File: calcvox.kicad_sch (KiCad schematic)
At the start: 146 parts, among them J1 AudioJack2_Ground_Switch, SW1 RotaryEncoder_Switch, SW10 SW_Push, SW11 SW_Push, SW12 SW_Push, SW13 SW_Push, SW14 SW_Push, SW15 SW_Push, SW16 SW_Push, SW17 SW_Push, SW18 SW_Push, SW19 SW_Push, SW2 SW_Push, SW20 SW_Push, SW21 SW_Push, SW22 SW_Push, SW23 SW_Push, SW24 SW_Push, SW25 SW_Push, SW26 SW_Push, SW27 SW_Push, SW28 SW_Push, SW29 SW_Push, SW3 SW_Push, SW30 SW_Push, SW31 SW_Push, SW32 SW_Push, SW33 SW_Push, SW34 SW_Push, SW35 SW_Push, SW36 SW_Push, SW37 SW_Push, SW38 SW_Push, SW39 SW_Push, SW4 SW_Push, SW40 SW_Push, SW41 SW_Push, SW42 SW_Push, SW43 SW_Push, SW44 SW_Push, SW45 SW_Push, SW46 SW_Push, SW47 SW_Push, SW48 SW_Push, SW49 SW_Push, SW5 SW_Push, SW50 SW_Push, SW51 SW_Push, SW52 SW_Push, SW53 SW_Push, SW54 SW_Push, SW55 SW_Push, SW56 SW_Push, SW57 SW_Push, SW58 SW_Push, SW59 SW_Push, SW6 SW_Push, SW60 SW_Push, SW61 SW_Push, SW62 SW_Push, SW63 SW_Push, SW64 SW_Push, SW65 SW_Push, SW66 SW_Push, SW67 SW_SPDT, SW7 SW_Push, SW8 SW_Push, SW9 SW_Push

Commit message: added new changes
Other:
- note added: "CalcVox"

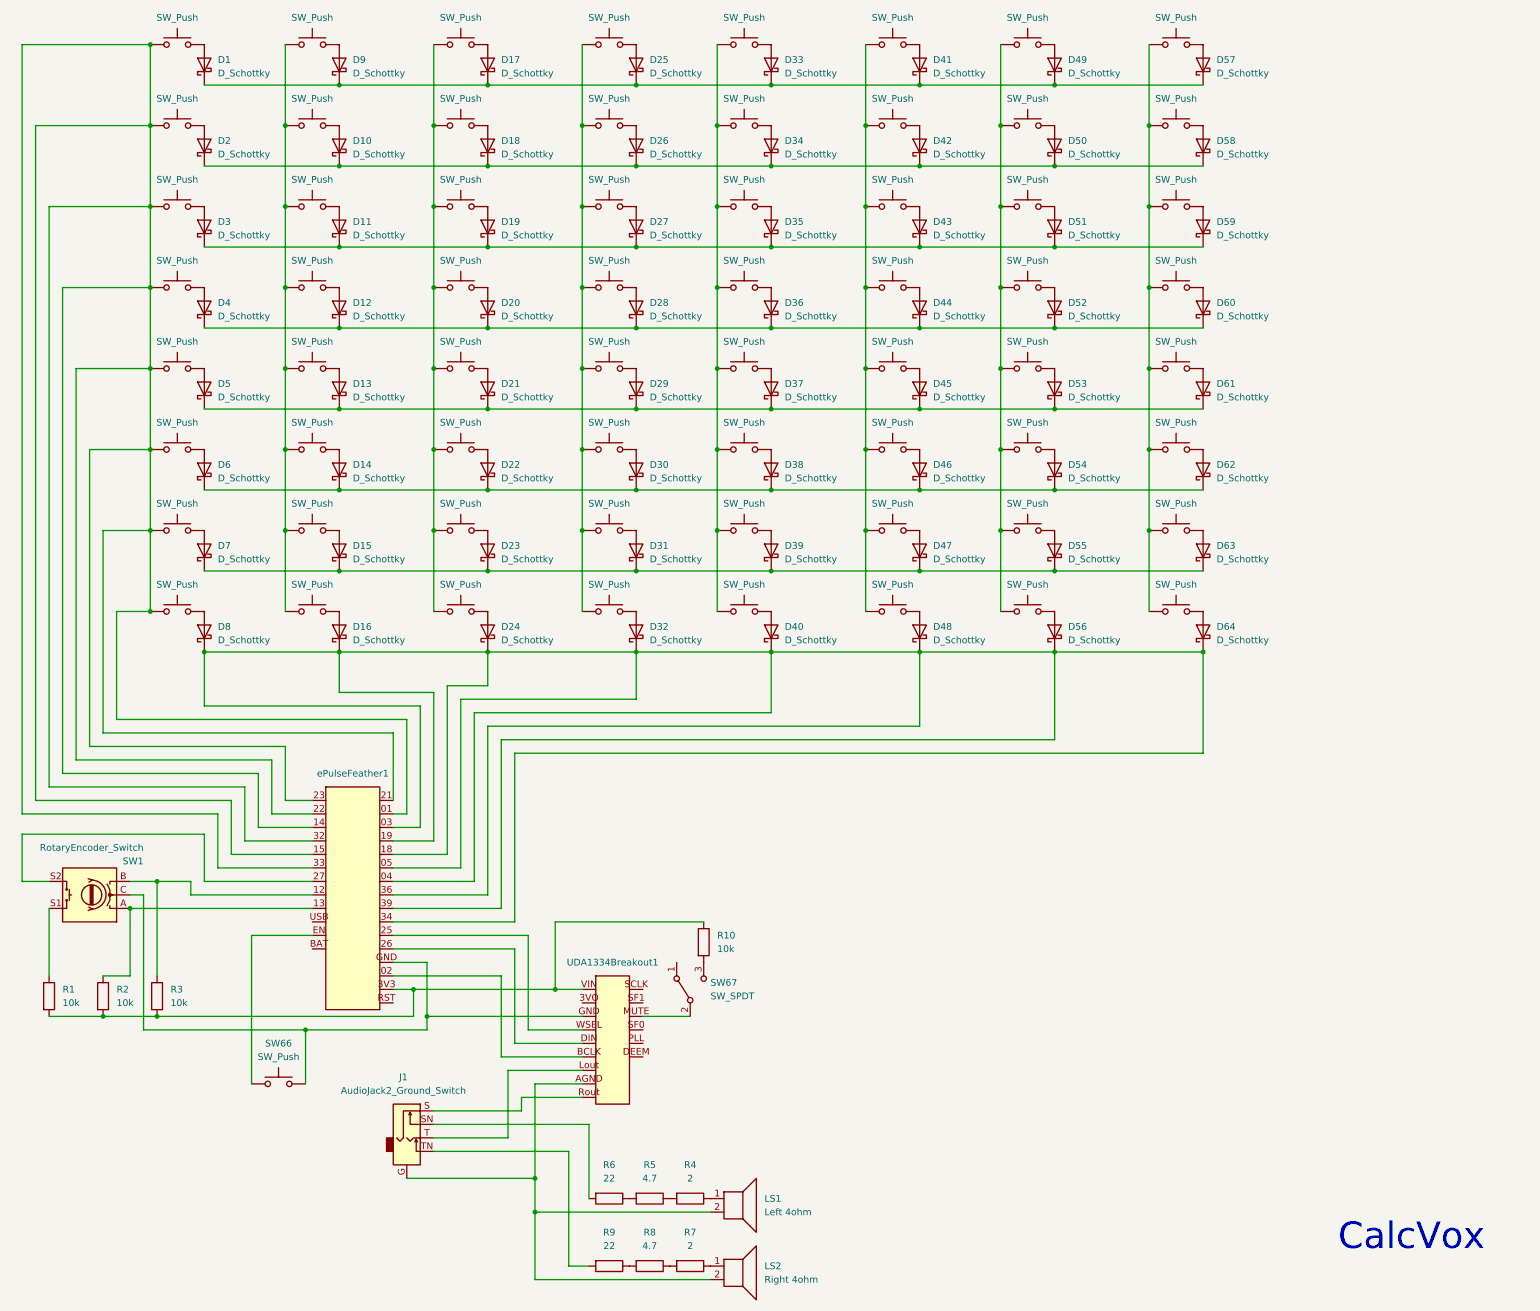
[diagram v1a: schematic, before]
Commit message: updated schematics
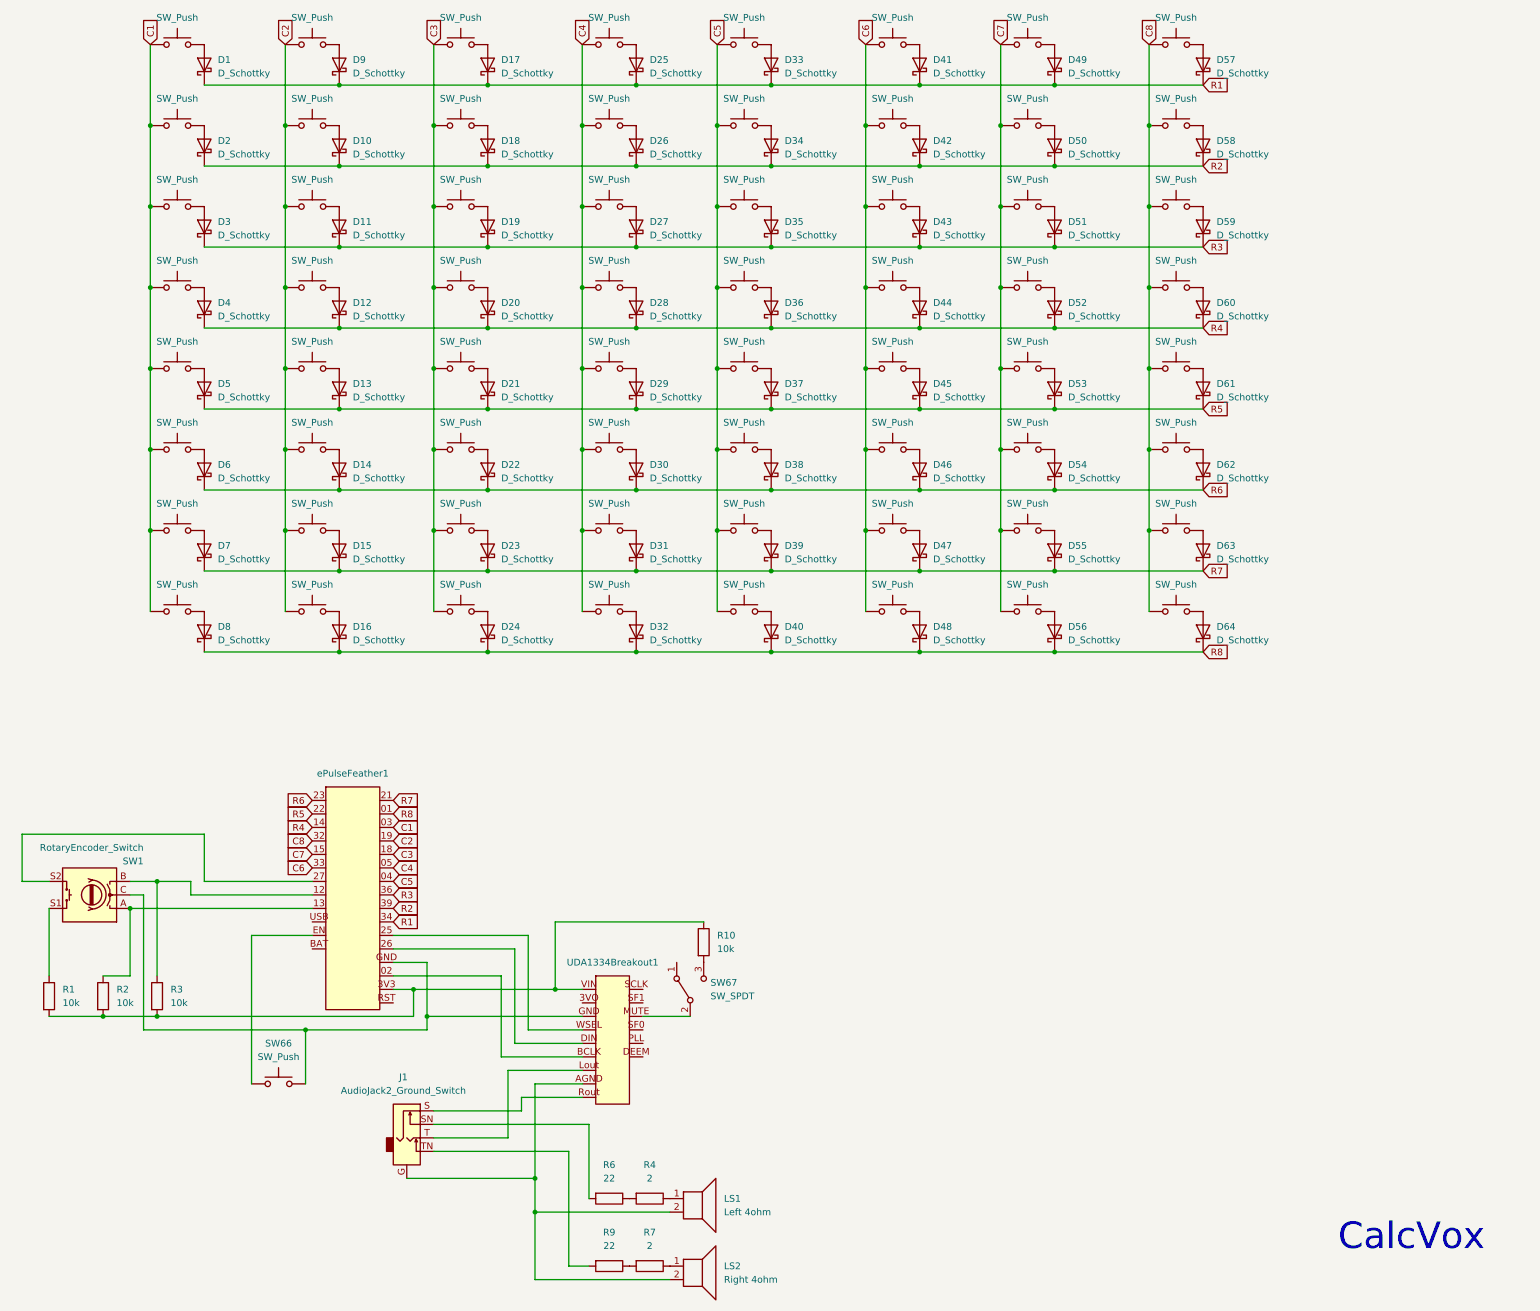
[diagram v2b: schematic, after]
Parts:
- removed R5, R8: 4.7, Resistor_THT:R_Axial_DIN0207_L6.3mm_D2.5mm_P7.62mm_Horizontal, symbol Device:R
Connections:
- net C4: now reaches SW26.1, SW27.1, SW28.1, SW29.1, SW30.1, SW31.1, SW32.1, SW33.1
- net C4: now also ePulseFeather1.05
- net R4: now reaches D12.1 (K), D20.1 (K), D28.1 (K), D36.1 (K), D4.1 (K), D44.1 (K), D52.1 (K), D60.1 (K)
- net R4: now also ePulseFeather1.14
- net R7: now reaches D15.1 (K), D23.1 (K), D31.1 (K), D39.1 (K), D47.1 (K), D55.1 (K), D63.1 (K), D7.1 (K)
- net R7: now also ePulseFeather1.21
- net R5: now reaches D13.1 (K), D21.1 (K), D29.1 (K), D37.1 (K), D45.1 (K), D5.1 (K), D53.1 (K), D61.1 (K)
- net R5: now also ePulseFeather1.22
- net R8: now reaches D16.1 (K), D24.1 (K), D32.1 (K), D40.1 (K), D48.1 (K), D56.1 (K), D64.1 (K), D8.1 (K)
- net R8: now also ePulseFeather1.01; no longer ePulseFeather1.03, ePulseFeather1.04, ePulseFeather1.05, ePulseFeather1.18, ePulseFeather1.19, ePulseFeather1.34, ePulseFeather1.36, ePulseFeather1.39
- net R2: now reaches D10.1 (K), D18.1 (K), D2.1 (K), D26.1 (K), D34.1 (K), D42.1 (K), D50.1 (K), D58.1 (K)
- net R2: now also ePulseFeather1.39
- net R1: now reaches D1.1 (K), D17.1 (K), D25.1 (K), D33.1 (K), D41.1 (K), D49.1 (K), D57.1 (K), D9.1 (K)
- net R1: now also ePulseFeather1.34
- net C1: now reaches SW2.1, SW3.1, SW4.1, SW5.1, SW6.1, SW7.1, SW8.1, SW9.1
- net C1: now also ePulseFeather1.03; no longer ePulseFeather1.01, ePulseFeather1.14, ePulseFeather1.15, ePulseFeather1.21, ePulseFeather1.22, ePulseFeather1.23, ePulseFeather1.32, ePulseFeather1.33
- net at R4.2: now also R6.1
- net C8: now reaches SW58.1, SW59.1, SW60.1, SW61.1, SW62.1, SW63.1, SW64.1, SW65.1
- net C8: now also ePulseFeather1.32
- net C2: now reaches SW10.1, SW11.1, SW12.1, SW13.1, SW14.1, SW15.1, SW16.1, SW17.1
- net C2: now also ePulseFeather1.19
- net R3: now reaches D11.1 (K), D19.1 (K), D27.1 (K), D3.1 (K), D35.1 (K), D43.1 (K), D51.1 (K), D59.1 (K)
- net R3: now also ePulseFeather1.36
- net R6: now reaches D14.1 (K), D22.1 (K), D30.1 (K), D38.1 (K), D46.1 (K), D54.1 (K), D6.1 (K), D62.1 (K)
- net R6: now also ePulseFeather1.23
- net C5: now reaches SW34.1, SW35.1, SW36.1, SW37.1, SW38.1, SW39.1, SW40.1, SW41.1
- net C5: now also ePulseFeather1.04
- net C3: now reaches SW18.1, SW19.1, SW20.1, SW21.1, SW22.1, SW23.1, SW24.1, SW25.1
- net C3: now also ePulseFeather1.18
- net C7: now reaches SW50.1, SW51.1, SW52.1, SW53.1, SW54.1, SW55.1, SW56.1, SW57.1
- net C7: now also ePulseFeather1.15
- net C6: now reaches SW42.1, SW43.1, SW44.1, SW45.1, SW46.1, SW47.1, SW48.1, SW49.1
- net C6: now also ePulseFeather1.33
- net at R7.2: now also R9.1
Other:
- moved on the sheet: LS1, LS2, R4, R7
